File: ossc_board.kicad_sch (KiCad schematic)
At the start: 4 parts

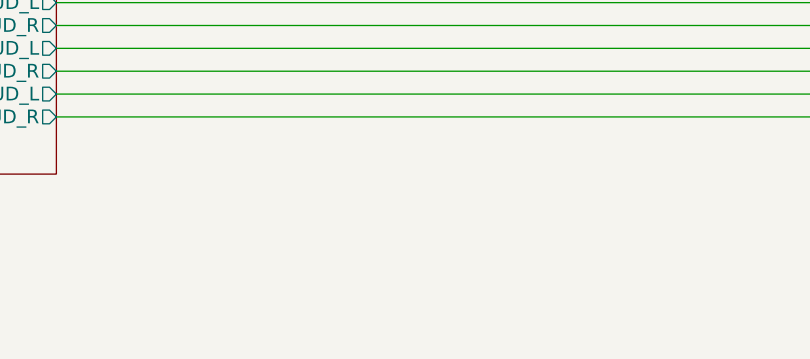
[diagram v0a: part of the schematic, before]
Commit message: change PCB version indicator pin due to conflict
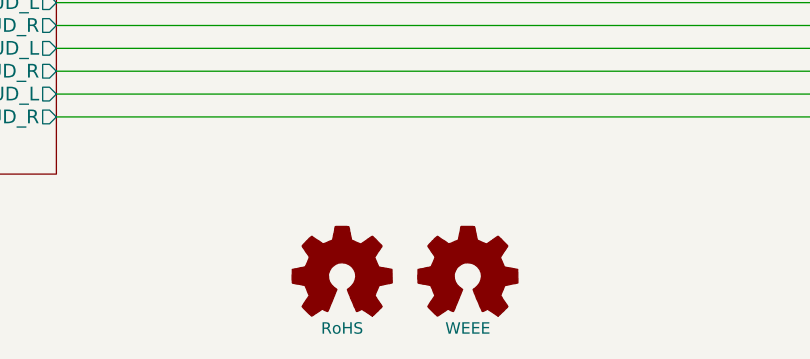
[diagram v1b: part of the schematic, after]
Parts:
- added G1: RoHS, custom_components:RoHS-logo, symbol Graphic:Logo_Open_Hardware_Small
- added G2: WEEE, custom_components:WEEE-logo, symbol Graphic:Logo_Open_Hardware_Small
- MH1, MH2, MH3, MH4: now left out of the parts list
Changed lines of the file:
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@@
   )
   (symbol (lib_id "Mechanical:MountingHole") (at 31.75 24.13 90) (unit 1)
-    (in_bom yes) (on_board yes) (dnp no)
+    (in_bom no) (on_board yes) (dnp no)
     (property "Reference" "MH1" (at 31.75 22.098 0)
       (effects (font (size 1.016 1.016)) (justify left))
@@
   )
   (symbol (lib_id "Mechanical:MountingHole") (at 34.29 158.75 90) (unit 1)
-    (in_bom yes) (on_board yes) (dnp no)
+    (in_bom no) (on_board yes) (dnp no)
     (property "Reference" "MH3" (at 34.29 156.718 0)
       (effects (font (size 1.016 1.016)) (justify left))
@@
   )
   (symbol (lib_id "Mechanical:MountingHole") (at 265.43 25.4 90) (unit 1)
-    (in_bom yes) (on_board yes) (dnp no)
+    (in_bom no) (on_board yes) (dnp no)
     (property "Reference" "MH2" (at 265.43 23.368 0)
       (effects (font (size 1.016 1.016)) (justify left))
@@
   )
   (symbol (lib_id "Mechanical:MountingHole") (at 264.16 157.48 90) (unit 1)
-    (in_bom yes) (on_board yes) (dnp no)
+    (in_bom no) (on_board yes) (dnp no)
     (property "Reference" "MH4" (at 264.16 155.448 0)
       (effects (font (size 1.016 1.016)) (justify left))
@@
         )
       )
+    )
+  )
+  (symbol (lib_id "Graphic:Logo_Open_Hardware_Small") (at 123.19 185.42 0) (unit 1)
+    (in_bom no) (on_board yes) (dnp no) (fields_autoplaced)
+    (property "Reference" "G2" (at 123.19 178.435 0)
+      (effects (font (size 1.27 1.27)) hide)
+    )
+    (property "Value" "WEEE" (at 123.19 191.135 0)
+      (effects (font (size 1.27 1.27)))
+    )
+    (property "Footprint" "custom_components:WEEE-logo" (at 123.19 185.42 0)
+      (effects (font (size 1.27 1.27)) hide)
+    )
+    (property "Datasheet" "~" (at 123.19 185.42 0)
+      (effects (font (size 1.27 1.27)) hide)
+    )
+    (property "Sim.Enable" "0" (at 123.19 185.42 0)
+      (effects (font (size 1.27 1.27)) hide)
+    )
+    (instances
+      (project "ossc_board"
+        (path "/7617fb4c-5622-4dbc-87c9-3373ab01a33e"
+          (reference "G2") (unit 1)
+        )
+      )
+    )
+  )
+  (symbol (lib_id "Graphic:Logo_Open_Hardware_Small") (at 109.22 185.42 0) (unit 1)
+    (in_bom no) (on_board yes) (dnp no) (fields_autoplaced)
+    (property "Reference" "G1" (at 109.22 178.435 0)
+      (effects (font (size 1.27 1.27)) hide)
+    )
+    (property "Value" "RoHS" (at 109.22 191.135 0)
+      (effects (font (size 1.27 1.27)))
+    )
+    (property "Footprint" "custom_components:RoHS-logo" (at 109.22 185.42 0)
+      (effects (font (size 1.27 1.27)) hide)
+    )
+    (property "Datasheet" "~" (at 109.22 185.42 0)
+      (effects (font (size 1.27 1.27)) hide)
+    )
+    (property "Sim.Enable" "0" (at 109.22 185.42 0)
+      (effects (font (size 1.27 1.27)) hide)
+    )
+    (instances
+      (project "ossc_board"
+        (path "/7617fb4c-5622-4dbc-87c9-3373ab01a33e"
+          (reference "G1") (unit 1)
+        )
+      )
